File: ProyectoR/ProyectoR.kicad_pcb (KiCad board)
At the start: 2 copper layers, 16 parts, among them Q1 BC547, U1 4N25

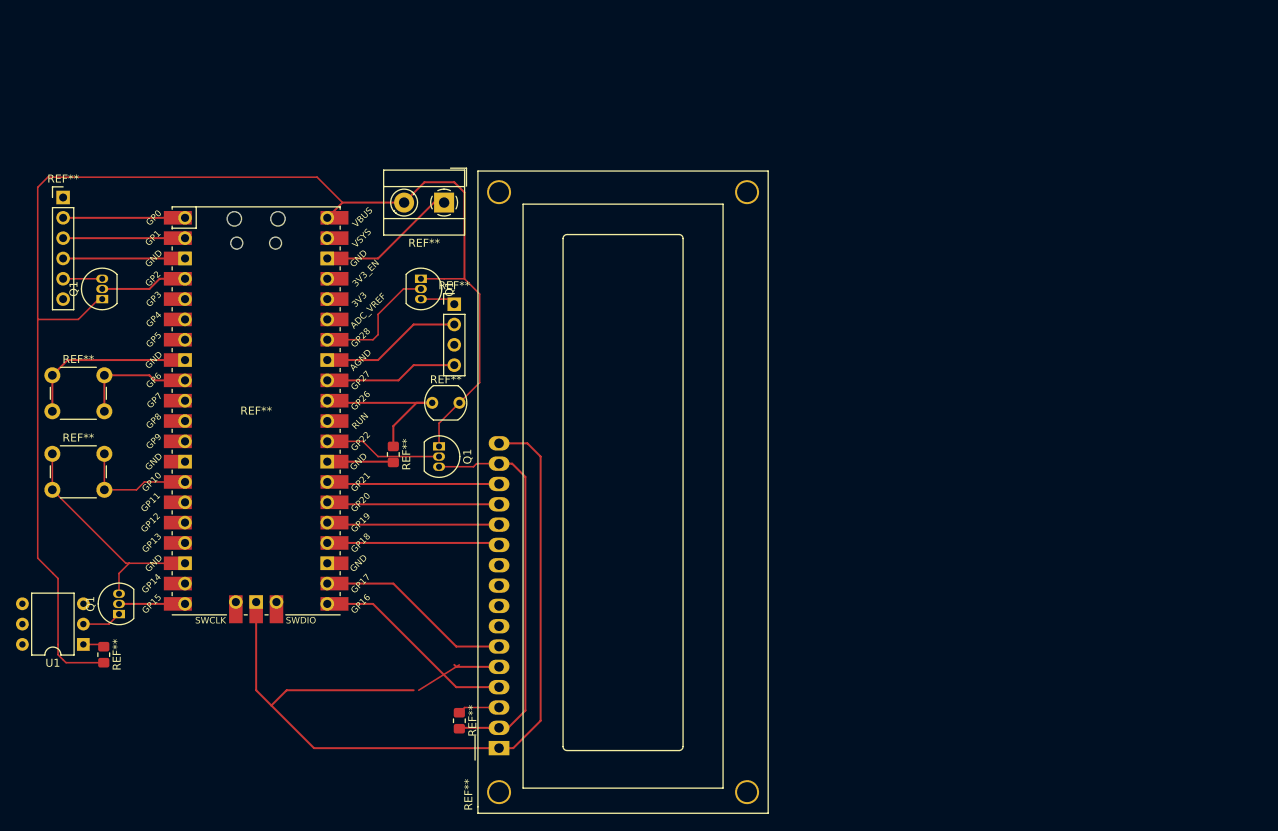
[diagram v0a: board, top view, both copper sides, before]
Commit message: Falta terminar
Acomodé la librería de footprints, cambié tierras con GND, cambié fotoresistor por pin de 2.54mm entre otro
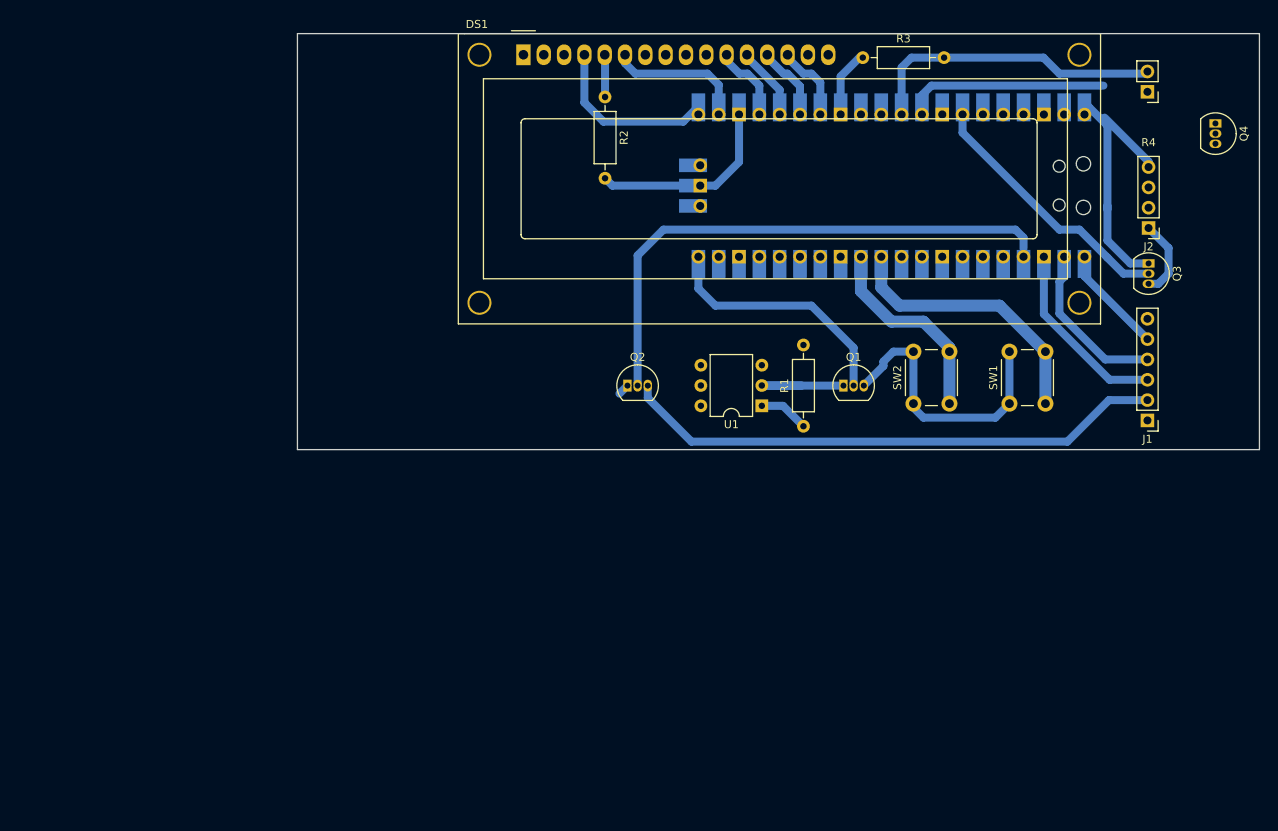
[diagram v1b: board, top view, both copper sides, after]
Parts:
- removed the Q1 at (169.2, 80.6)
- removed the Q1 at (131.4, 122.6)
- removed the Q1 at (129.3, 83.2)
- removed the Q1 at (171.4, 101.6)
- removed REF** (x3): ., Resistor_SMD:R_0805_2012Metric_Pad1.20x1.40mm_HandSolder
- removed REF**: RPi_Pico_SMD_TH, MCU_RaspberryPi_and_Boards:RPi_Pico_SMD_TH
- removed REF**: PinHeader_1x04_P2.54mm_Vertical, Connector_PinHeader_2.54mm:PinHeader_1x04_P2.54mm_Vertical
- removed REF**: TerminalBlock_MetzConnect_Type055_RT01502HDWU_1x02_P5.00mm_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, TerminalBlock_MetzConnect:TerminalBlock_MetzConnect_Type055_RT01502HDWU_1x02_P5.00mm_Horizontal
- removed REF**: ., OptoDevice:R_LDR_5.1x4.3mm_P3.4mm_Vertical
- removed REF** (x2): SW_PUSH_6mm_H5mm, Button_Switch_THT:SW_PUSH_6mm_H5mm
- removed REF**: WC1602A, Display:WC1602A
- removed REF**: PinHeader_1x06_P2.54mm_Vertical, Connector_PinHeader_2.54mm:PinHeader_1x06_P2.54mm_Vertical
- added DS1: WC1602A, Display:WC1602A, F.Cu at (182.0, 52.6)
- added J1: Conn_01x06, Connector_PinHeader_2.54mm:PinHeader_1x06_P2.54mm_Vertical, F.Cu at (260.0, 98.3)
- added J2: Conn_01x04, Connector_PinHeader_2.54mm:PinHeader_1x04_P2.54mm_Vertical, F.Cu at (260.1, 74.3)
- added Q1: BC547, Package_TO_SOT_THT:TO-92_Inline, F.Cu at (222.0, 94.0)
- added Q2: BC547, Package_TO_SOT_THT:TO-92_Inline, F.Cu at (195.0, 94.0)
- added Q3: BC547, Package_TO_SOT_THT:TO-92_Inline, F.Cu at (260.1, 78.7)
- added Q4: BC547, Package_TO_SOT_THT:TO-92_Inline, F.Cu at (268.5, 61.2)
- added R1: R, Resistor_THT:R_Axial_DIN0207_L6.3mm_D2.5mm_P10.16mm_Horizontal, F.Cu at (217.0, 99.1)
- added R2: R, Resistor_THT:R_Axial_DIN0207_L6.3mm_D2.5mm_P10.16mm_Horizontal, F.Cu at (192.2, 57.9)
- added R3: R, Resistor_THT:R_Axial_DIN0207_L6.3mm_D2.5mm_P10.16mm_Horizontal, F.Cu at (224.4, 53.0)
- added R4: R_Photo, Connector_PinHeader_2.54mm:PinHeader_1x02_P2.54mm_Vertical, F.Cu at (260.0, 57.3)
- added SW1: SW_DIP_x01, Button_Switch_THT:SW_PUSH_6mm_H5mm, F.Cu at (242.8, 96.2)
- added SW2: SW_DIP_x01, Button_Switch_THT:SW_PUSH_6mm_H5mm, F.Cu at (230.8, 96.2)
- added U2: Pico, Librerias kicad:RPi_Pico_SMD_TH, B.Cu at (228.0, 69.0)
- moved U1 89.9 mm to (211.8, 96.5)
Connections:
- U1 pad 1: (no net) -> Net-(R1-Pad1)
- U1 pad 2: (no net) -> Net-(Q1-Pad1)
- U1 pad 3: (no net) -> unconnected-(U1-Pad3)
- U1 pad 4: (no net) -> unconnected-(U1-Pad4)
- U1 pad 5: (no net) -> unconnected-(U1-Pad5)
- U1 pad 6: (no net) -> unconnected-(U1-Pad6)
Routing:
- net (no net): track 755.9 -> 0.00 mm
- net GND: track 0.00 -> 91.3 mm
- net Net-(J1-Pad2): track 0.00 -> 68.4 mm
- net Net-(Q2-Pad2): track 0.00 -> 67.6 mm
- net Net-(R4-Pad2): track 0.00 -> 37.3 mm
- net Net-(SW1-Pad2): track 0.00 -> 34.2 mm
- net Net-(Q3-Pad2): track 0.00 -> 33.8 mm
- net Net-(J2-Pad4): track 0.00 -> 33.1 mm
- net Net-(Q1-Pad2): track 0.00 -> 31.2 mm
- net +5V: track 0.00 -> 26.5 mm
- net Net-(SW2-Pad2): track 0.00 -> 25.3 mm
- net Net-(DS1-Pad4): track 0.00 -> 22.0 mm
- net Net-(J1-Pad4): track 0.00 -> 20.7 mm
- net Net-(DS1-Pad6): track 0.00 -> 16.6 mm
- net Net-(Q1-Pad1): track 0.00 -> 15.2 mm
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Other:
- board outline added: 120.2 x 52 mm

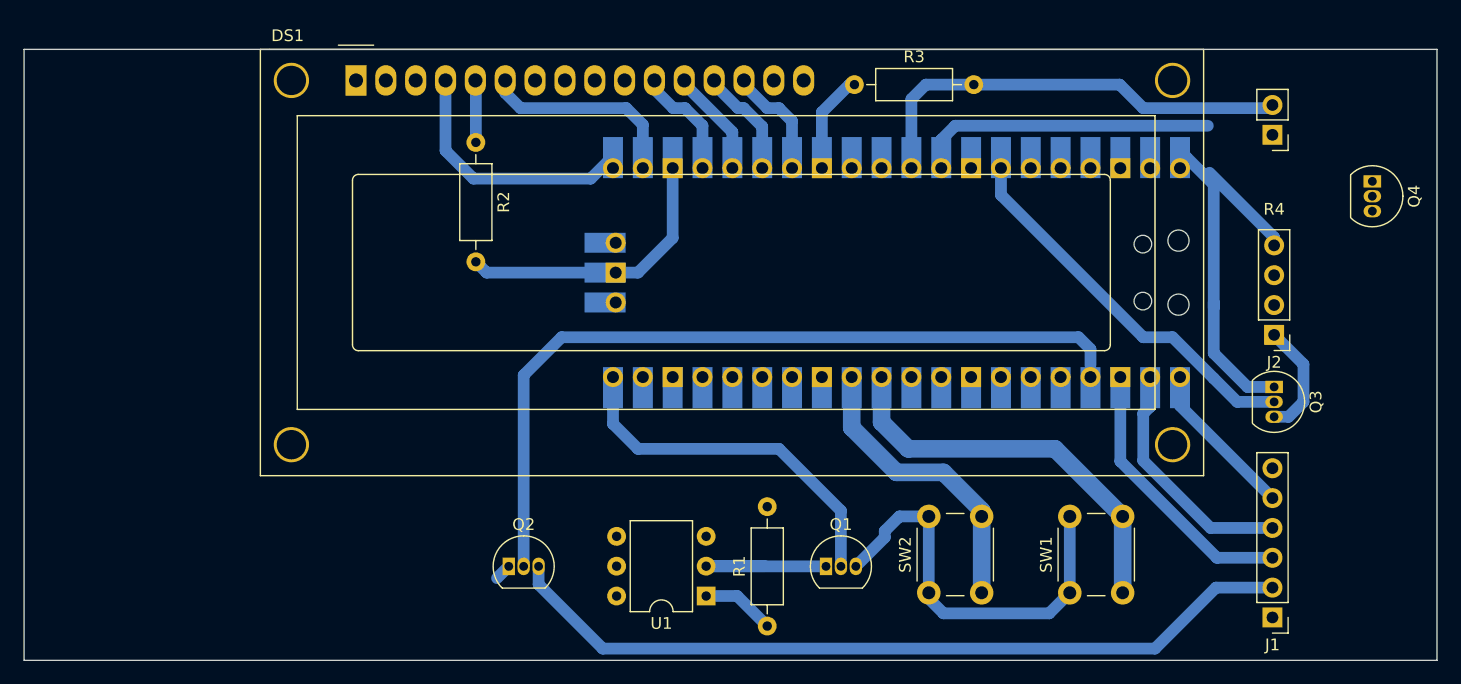
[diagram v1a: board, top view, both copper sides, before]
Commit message: V1.0.0
Terminé el pcb, quedó con tres puentes nomás
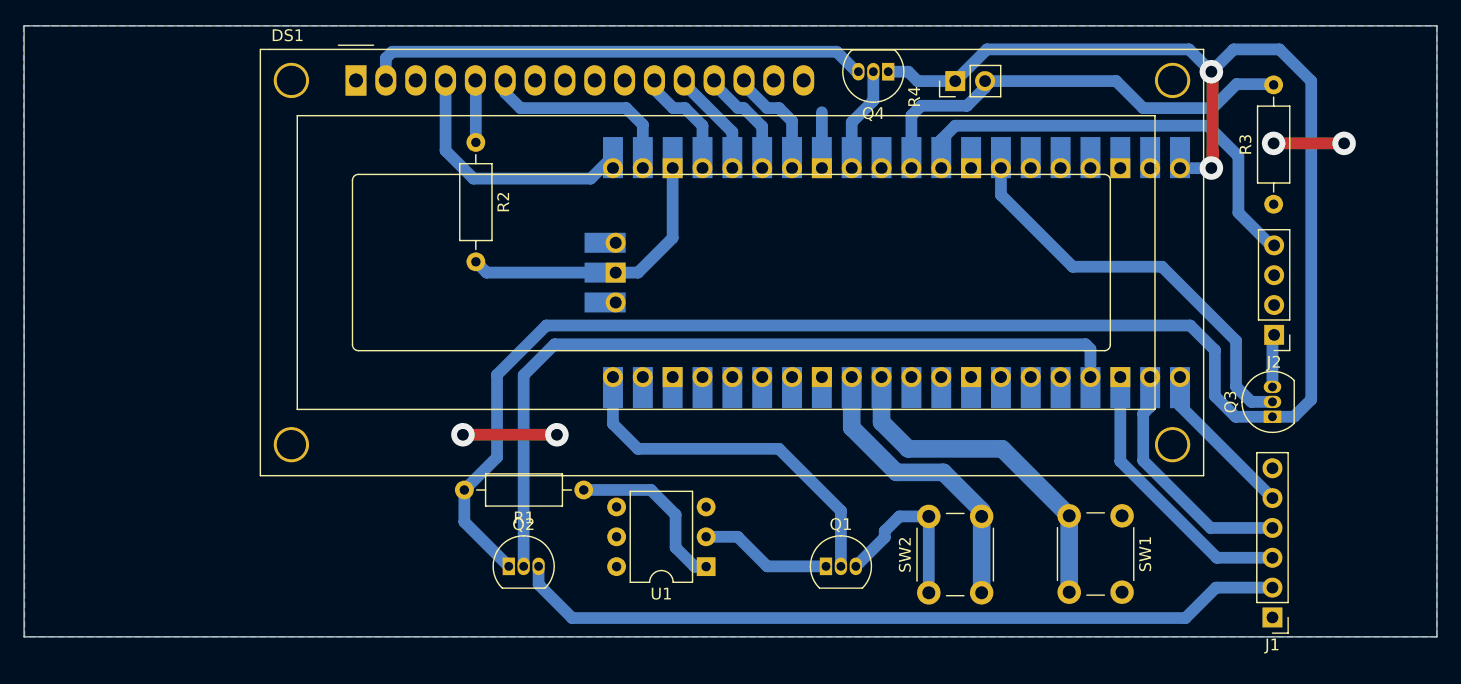
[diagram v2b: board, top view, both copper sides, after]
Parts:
- moved Q4 42.2 mm to (227.3, 51.9), turned to 180 degrees
- moved R3 37.1 mm to (260.1, 63.2), turned to 90 degrees
- moved R4 27.4 mm to (233.0, 52.7), turned to 90 degrees
- moved R1 19.4 mm to (201.4, 87.5), turned to 180 degrees
- moved SW1 7.92 mm to (247.2, 89.7), turned to -90 degrees
- moved Q3 2.54 mm to (260.0, 81.3), turned to 90 degrees
- moved U1 2.50 mm to (211.8, 94.0)
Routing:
- net +5V: track 26.5 -> 176.9 mm, vias 0 -> 2
- net Net-(DS1-Pad2): track 0.00 -> 43.0 mm
- net GND: track 91.3 -> 81.9 mm, vias 0 -> 4
- net Net-(Q4-Pad2): track 0.00 -> 8.97 mm
- net Net-(R1-Pad1): track 6.26 -> 14.8 mm
- net Net-(J2-Pad1): track 9.76 -> 4.49 mm
- net Net-(SW1-Pad2): track 34.2 -> 29.6 mm
- net Net-(J2-Pad4): track 33.1 -> 37.3 mm
- net Net-(Q1-Pad1): track 15.2 -> 11.2 mm
- net Net-(Q3-Pad2): track 33.8 -> 36.1 mm
- net Net-(J1-Pad2): track 68.4 -> 66.3 mm
- net Net-(R3-Pad2): track 37.3 -> 38.8 mm
- added copper zone on B.Cu, net GND

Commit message: Add files via upload
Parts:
- added J3: Screw_Terminal_01x02, TerminalBlock_Philmore:TerminalBlock_Philmore_TB132_1x02_P5.00mm_Horizontal, F.Cu at (267.9, 83.3)
- added J4: Screw_Terminal_01x02, TerminalBlock_Philmore:TerminalBlock_Philmore_TB132_1x02_P5.00mm_Horizontal, F.Cu at (181.6, 96.0)
- U1: value 4N25 -> MOC3023M
- moved R2 5.28 mm to (186.9, 58.4)
- moved Q1 0.78 mm to (222.8, 93.8)
- moved U1 0.50 mm to (211.6, 94.5)
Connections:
- DS1 pad 3: unconnected-(DS1-Pad3) -> Net-(DS1-Pad3)
- DS1 pad 5: Net-(DS1-Pad5) -> GND
- Q1 pad 2: Net-(Q1-Pad2) -> Net-(U2-Pad12)
- R2 pad 1: Net-(DS1-Pad5) -> Net-(DS1-Pad3)
- U1 pad 4: unconnected-(U1-Pad4) -> Net-(U1-Pad4)
- U1 pad 6: unconnected-(U1-Pad6) -> Net-(U1-Pad6)
- U2 pad 11: Net-(SW1-Pad2) -> unconnected-(U2-Pad11)
- U2 pad 12: Net-(SW2-Pad2) -> Net-(U2-Pad12)
- U2 pad 20: Net-(Q1-Pad2) -> Net-(Q2-Pad2)
- U2 pad 4: Net-(Q2-Pad2) -> unconnected-(U2-Pad4)
- U2 pad 5: unconnected-(U2-Pad5) -> Net-(SW1-Pad2)
- U2 pad 9: unconnected-(U2-Pad9) -> Net-(SW2-Pad2)
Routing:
- net GND: track 81.9 -> 33.2 mm
- net Net-(Q2-Pad2): track 67.1 -> 22.0 mm
- net Net-(Q1-Pad2): track 31.2 -> 0.00 mm
- net Net-(U1-Pad6): track 0.00 -> 23.5 mm, vias 0 -> 1
- net Net-(U1-Pad4): track 0.00 -> 23.0 mm, vias 0 -> 1
- net Net-(U2-Pad12): track 0.00 -> 16.0 mm
- net Net-(SW1-Pad2): track 29.6 -> 18.7 mm
- net +5V: track 176.9 -> 182.9 mm
- net Net-(DS1-Pad3): track 0.00 -> 5.83 mm
- net Net-(DS1-Pad5): track 5.29 -> 0.00 mm
- net Net-(SW2-Pad2): track 25.3 -> 20.3 mm

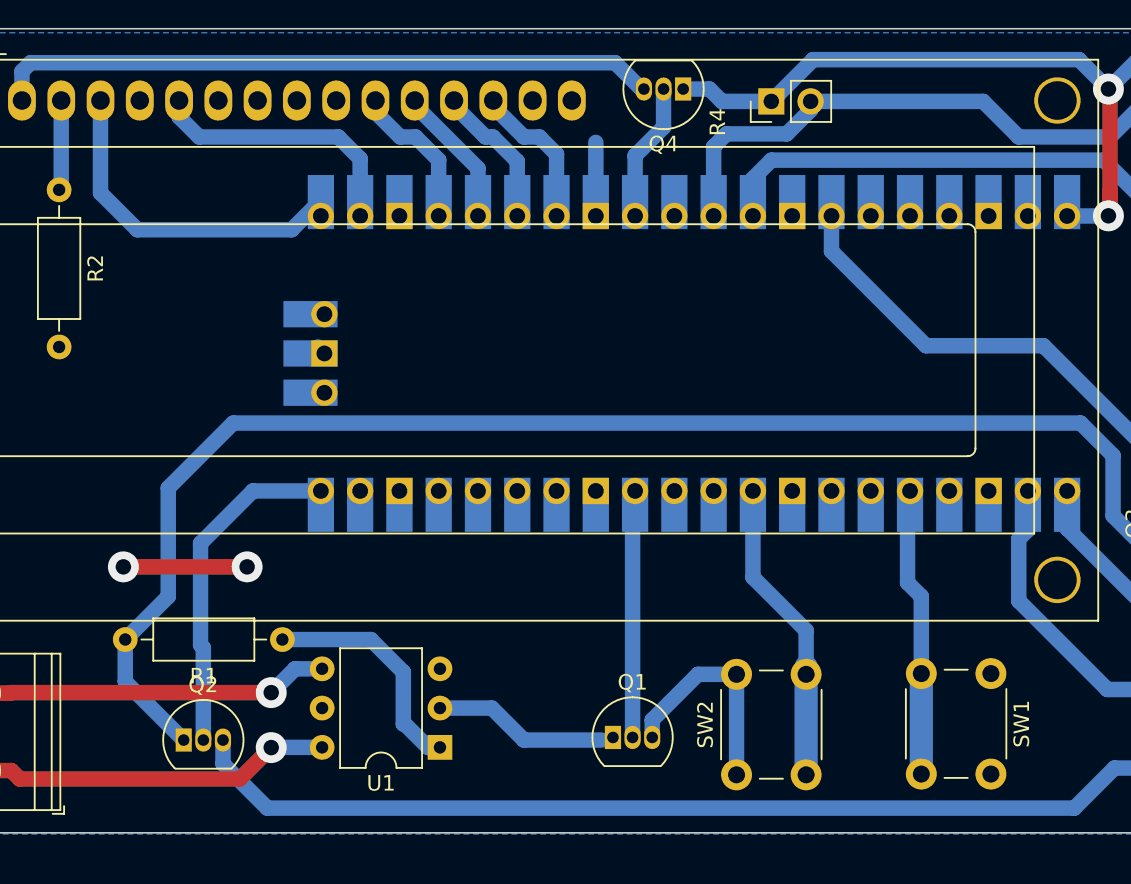
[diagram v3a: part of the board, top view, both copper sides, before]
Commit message: Aumento Clearance Power plane GND
Aumenté la distancia mínima entre el power plane de GND así será más fácil a la hora de fabricarlo
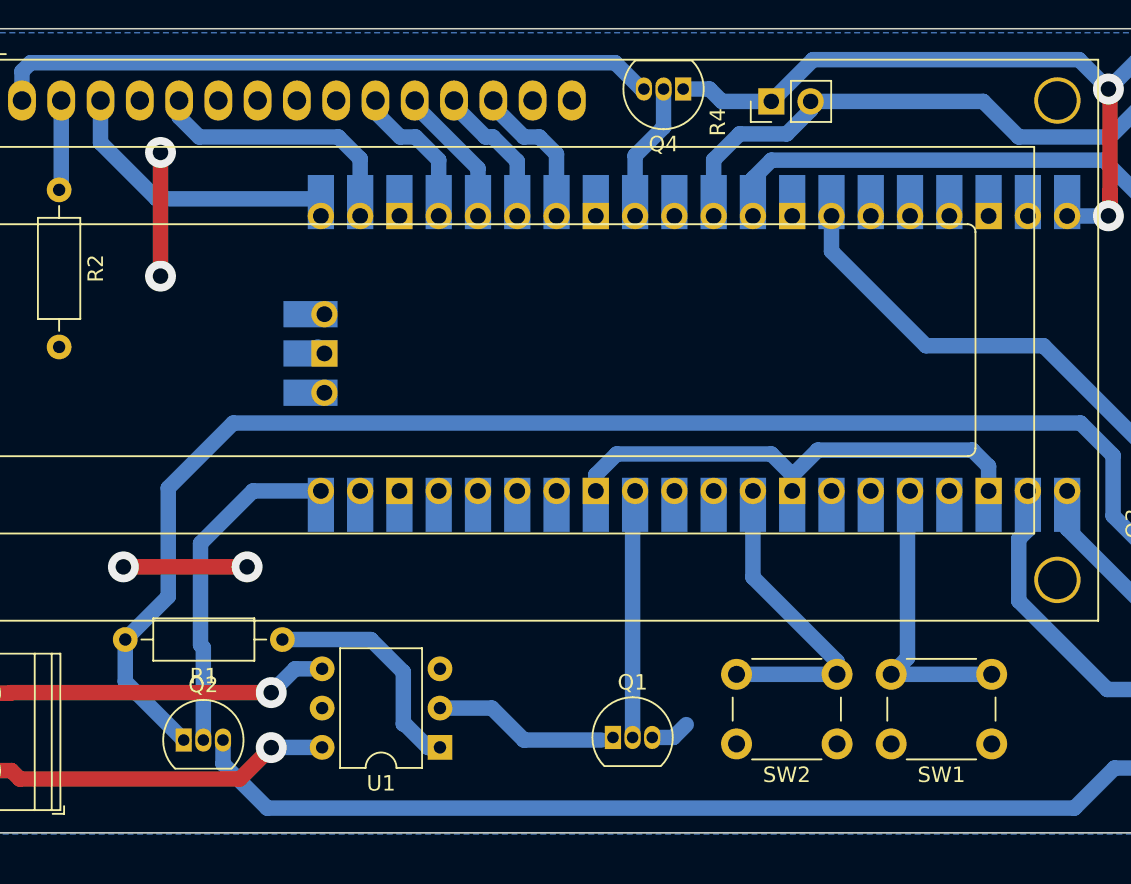
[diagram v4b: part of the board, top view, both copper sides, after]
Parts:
- moved SW2 6.80 mm to (237.2, 94.2), turned to 180 degrees
- moved SW1 4.55 mm to (247.2, 94.2), turned to 180 degrees
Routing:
- net GND: track 33.2 -> 57.5 mm, vias 4 -> 6
- net Net-(DS1-Pad4): track 22.0 -> 18.5 mm
